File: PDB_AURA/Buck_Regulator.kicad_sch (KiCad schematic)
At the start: 33 parts, among them Q1 CSD18540Q5B, Q2 CSD18510Q5B, U1 LM25145RGYR

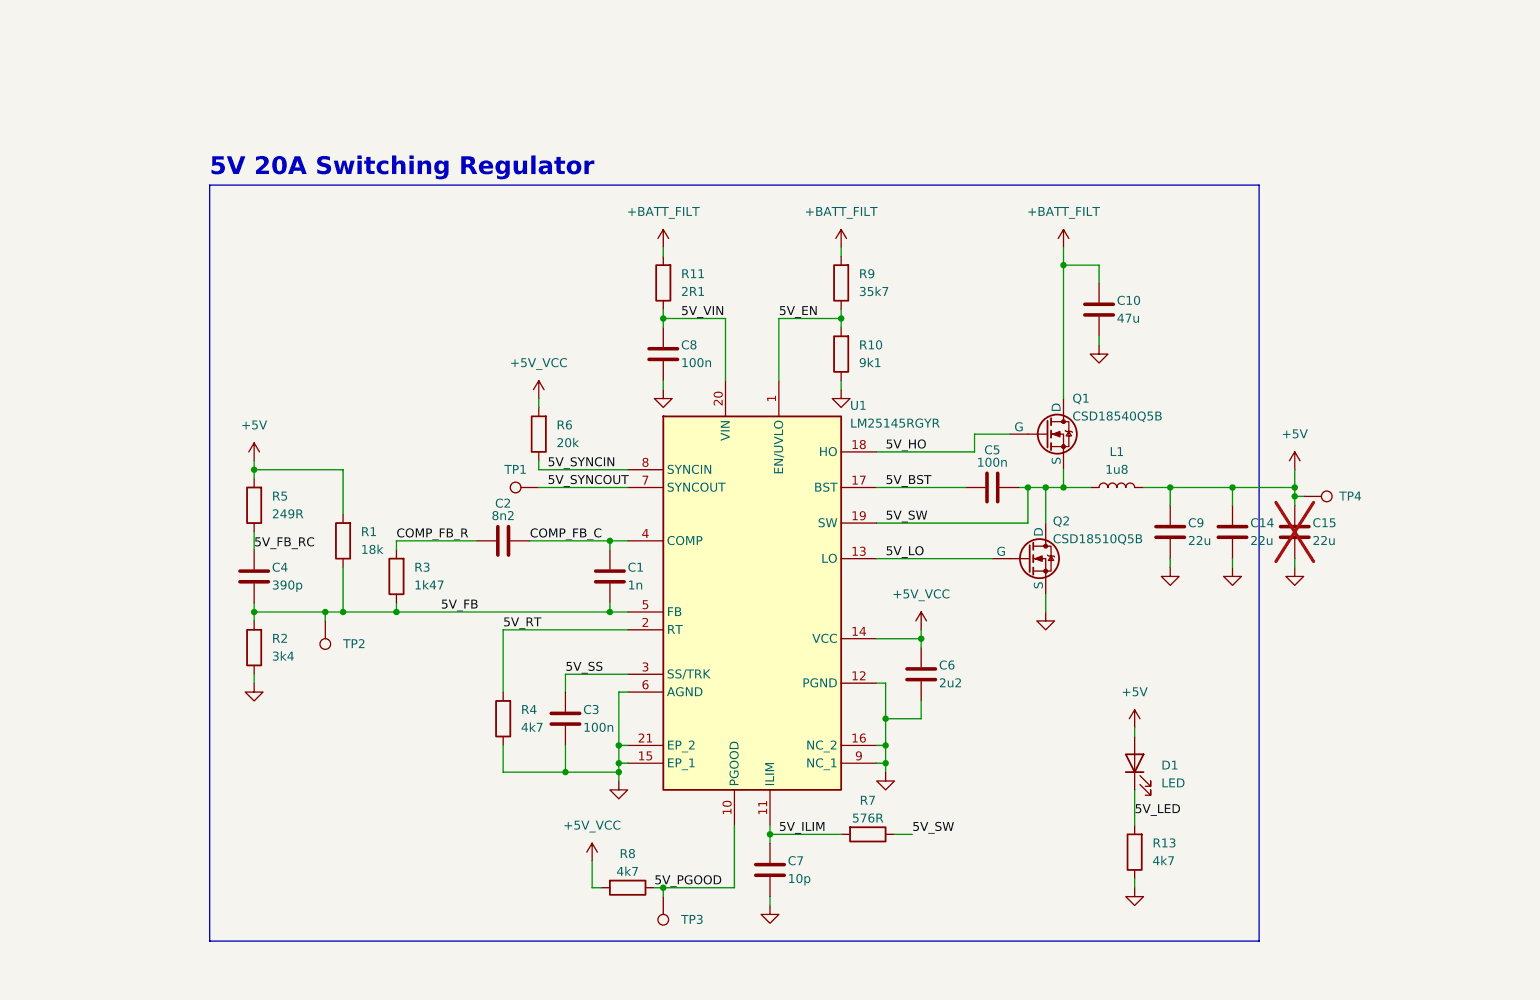
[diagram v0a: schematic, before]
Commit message: Annotated schematic for PDB
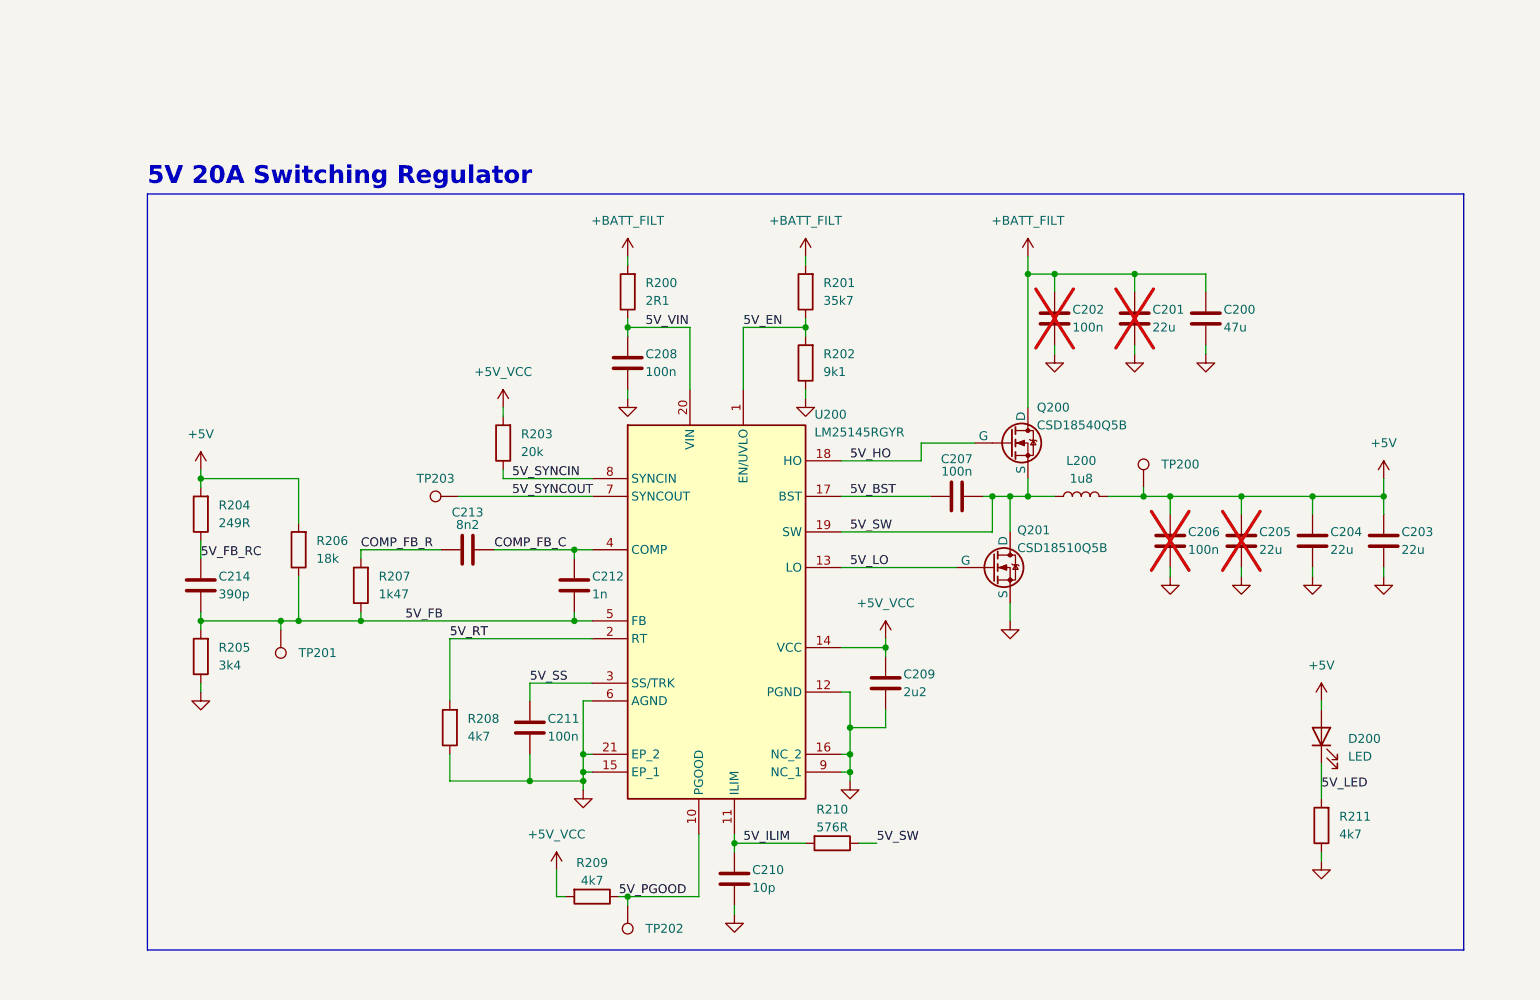
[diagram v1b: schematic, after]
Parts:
- added C201: 22u, Capacitor_SMD:C_1210_3225Metric, symbol Device:C
- added C202, C206: 100n, Capacitor_SMD:C_0402_1005Metric, symbol Device:C
- renumbered C10 to C200, C9 to C203, C14 to C204, C15 to C205, C5 to C207, C8 to C208, C6 to C209, C7 to C210, C3 to C211, C1 to C212, C2 to C213, C4 to C214, D1 to D200, L1 to L200, Q1 to Q200, Q2 to Q201, R11 to R200, R9 to R201, R10 to R202, R6 to R203, R5 to R204, R2 to R205, R1 to R206, R3 to R207, R4 to R208, R8 to R209, R7 to R210, R13 to R211, TP4 to TP200, TP2 to TP201, TP3 to TP202, TP1 to TP203, U1 to U200
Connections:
- net +5V: now also C206.1
- net +BATT_FILT: now also C201.1, C202.1
- net GND: now also C201.2, C202.2, C206.2
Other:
- title: (none) -> 5V 20A Switching Regulator
- moved on the sheet: C200, C203, C204, C205, C207, C208, C209, C210, C211, C212, C213, C214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

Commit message: Second Layout Attempt
Renamed all components and placed them all.
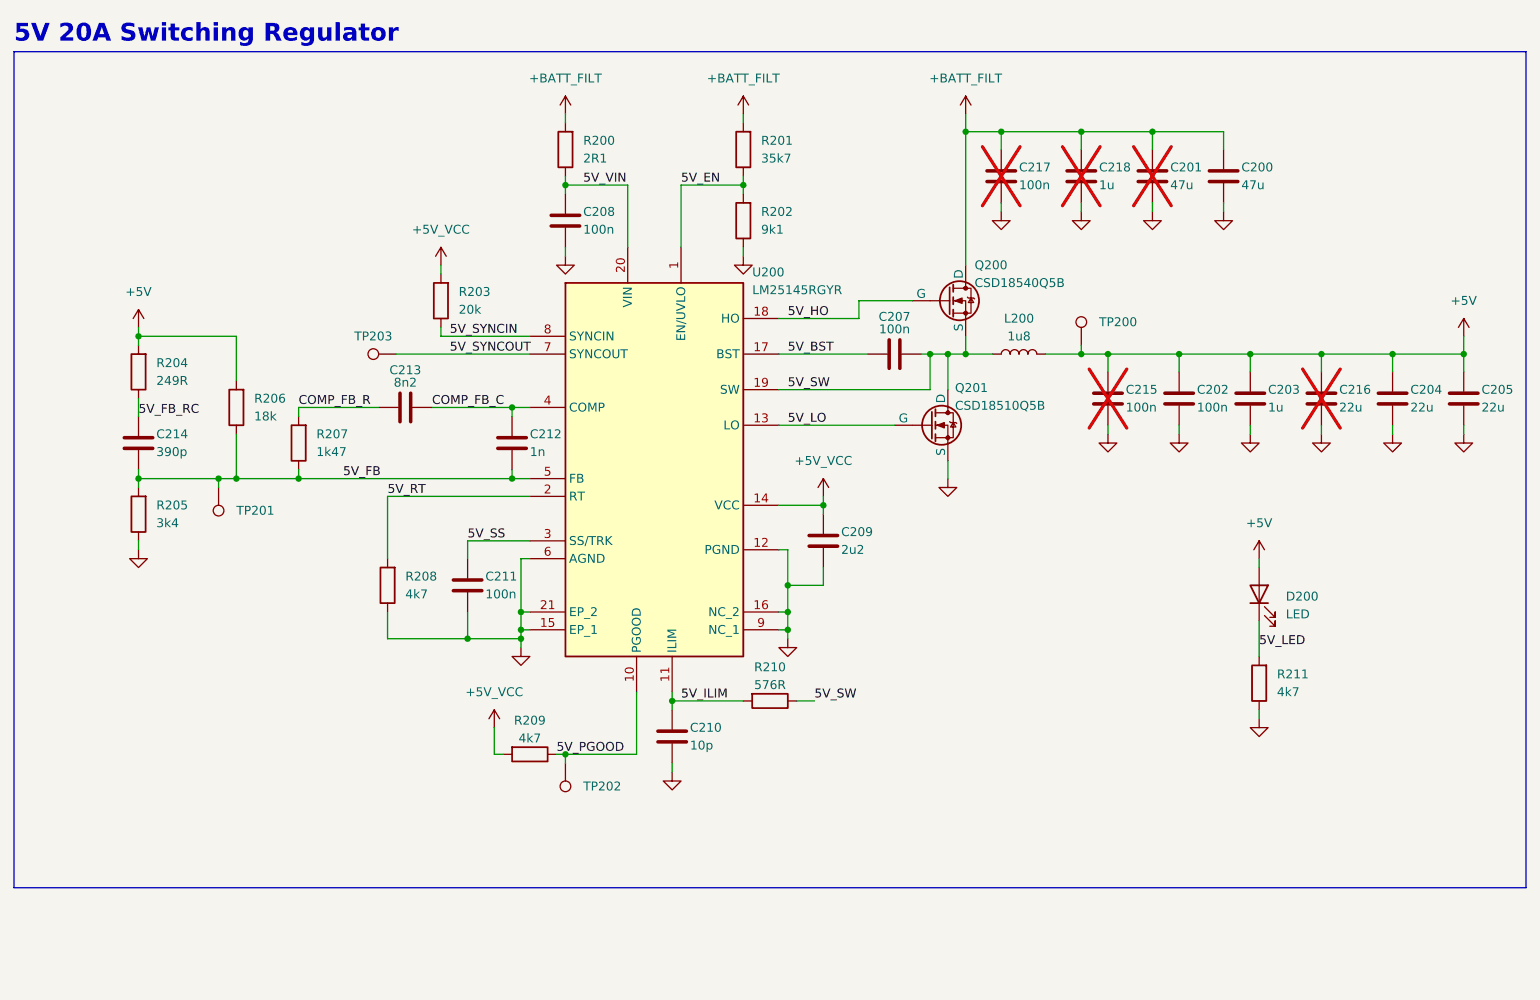
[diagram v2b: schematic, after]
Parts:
- added C202: 100n, Capacitor_SMD:C_0402_1005Metric, symbol Device:C
- added C203, C218: 1u, Capacitor_SMD:C_0402_1005Metric, symbol Device:C
- C201: value 22u -> 47u
- renumbered C203 to C205, C206 to C215, C205 to C216, C202 to C217
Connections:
- net +5V: now also C202.1, C203.1
- net +BATT_FILT: now also C218.1
- net GND: now also C202.2, C203.2, C218.2
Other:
- moved on the sheet: C200, C204, C205, C207, C208, C209, C210, C211, C212, C213, C214, C215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

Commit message: First PDB Version
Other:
- moved on the sheet: C200, C201, C202, C203, C204, C205, C207, C208, C209, C210, C211, C212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

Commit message: Second Iteration
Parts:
- C204, C205: value 22u -> 47u
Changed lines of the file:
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@@
 			)
 		)
-		(property "Value" "22u"
+		(property "Value" "47u"
 			(at 232.41 82.55 0)
 			(effects
@@
 			)
 		)
-		(property "Value" "22u"
+		(property "Value" "47u"
 			(at 242.57 82.55 0)
 			(effects

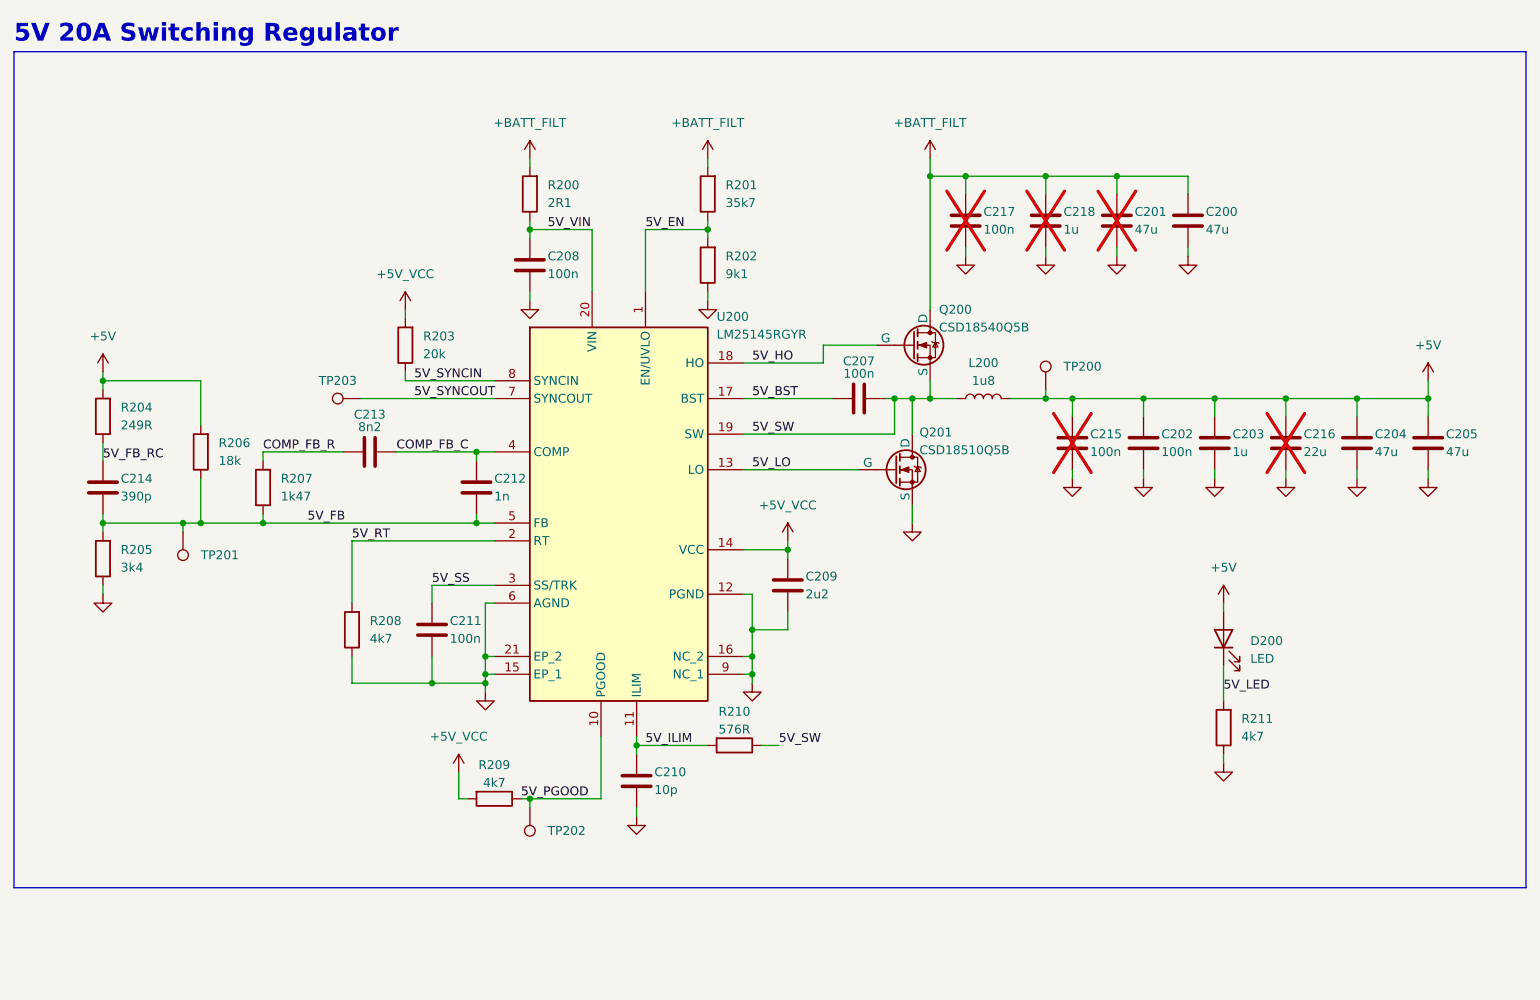
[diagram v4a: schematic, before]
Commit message: New Component Values
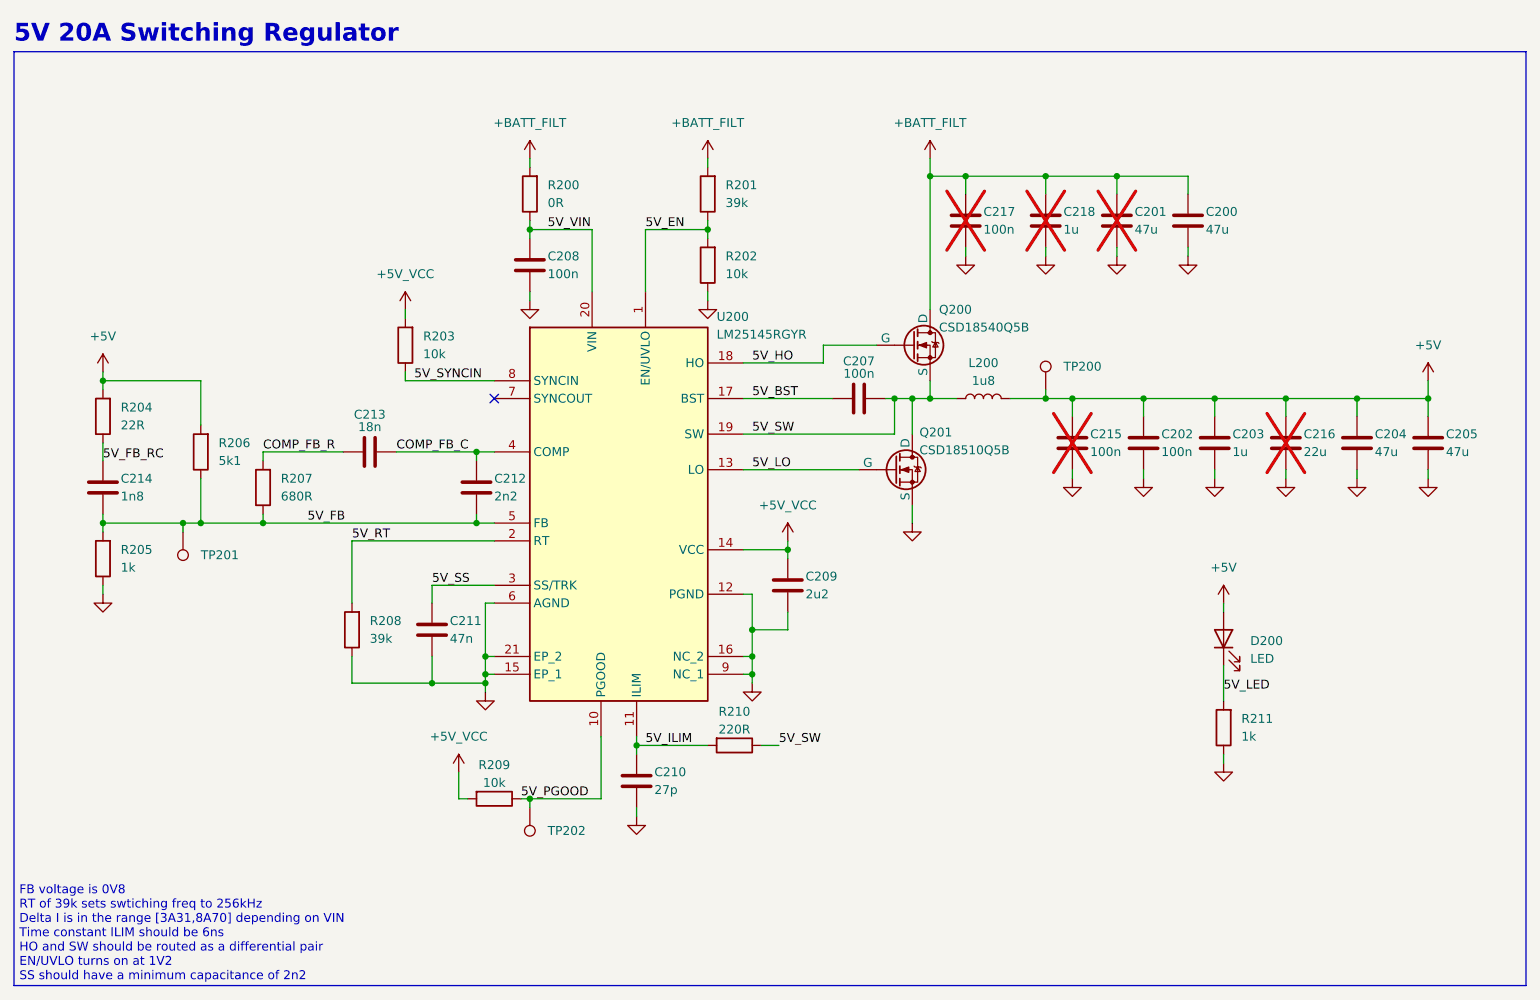
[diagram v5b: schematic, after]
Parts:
- removed TP203: TestPoint, TestPoint:TestPoint_Pad_D1.0mm, symbol Connector:TestPoint
- C210: value 10p -> 27p
- C211: value 100n -> 47n
- C212: value 1n -> 2n2
- C213: value 8n2 -> 18n
- C214: value 390p -> 1n8
- R200: value 2R1 -> 0R; JLCPCB (none) -> C25783
- R201: value 35k7 -> 39k; JLCPCB (none) -> C25783
- R202: value 9k1 -> 10k
- R203: value 20k -> 10k
- R204: value 249R -> 22R
- R205: value 3k4 -> 1k
- R206: value 18k -> 5k1
- R207: value 1k47 -> 680R
- R208: value 4k7 -> 39k; JLCPCB (none) -> C25783
- R209: value 4k7 -> 10k
- R210: value 576R -> 220R; JLCPCB (none) -> C25091
- R211: value 4k7 -> 1k
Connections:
- net 5V_SYNCOUT: no longer names the net of U200.7 (SYNCOUT)
- no-connect marks 0 -> 1
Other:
- note added: "FB voltage is 0V8 RT of 39k sets swtiching freq to 256kHz Delta I is in the range [3A31,8A70] depending on VIN Time constant ILIM should be 6ns HO and SW should be routed as a differential pair EN/UVLO turns on at 1V2 SS should have a minimum capacitance of 2n2"

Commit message: Second iteration PDB
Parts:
- C201, C215, C217, C218: now fitted; now in the parts list
- C212: value 2n2 -> 1n
- C216: value 22u -> 47u; now fitted; now in the parts list
- R207: value 680R -> 1k
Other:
- moved on the sheet: D200, R211

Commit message: PDB organised
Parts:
- C207: footprint Resistor_SMD:R_0402_1005Metric -> Capacitor_SMD:C_0402_1005Metric
- C210: value 27p -> 10p
- R205: value 1k -> 2k
- R206: value 5k1 -> 10k5
- R210: value 220R -> 470R
